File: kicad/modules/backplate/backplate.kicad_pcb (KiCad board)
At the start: 2 copper layers, 28 x 100 mm, 5 parts, among them J1 10018784-10210TLF

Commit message: update backplate libraries and schematic
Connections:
- J1 pad A10: unconnected-(J1-PadA10) -> +3.3V (x5)
- J1 pad A11: unconnected-(J1-PadA11) -> +3.3V (x5)
- J1 pad A12: unconnected-(J1-PadA12) -> +5V (x5)
- J1 pad A13: unconnected-(J1-PadA13) -> +5V (x5)
- J1 pad A14: unconnected-(J1-PadA14) -> +5V (x5)
- J1 pad A16: unconnected-(J1-PadA16) -> +7.4V (x5)
- J1 pad A17: unconnected-(J1-PadA17) -> +7.4V (x5)
- J1 pad A18: unconnected-(J1-PadA18) -> +7.4V (x5)
- J1 pad A2: unconnected-(J1-PadA2) -> CANP (x5)
- J1 pad A3: unconnected-(J1-PadA3) -> CANN (x5)
- J1 pad A4: unconnected-(J1-PadA4) -> GND (x5)
- J1 pad A5: unconnected-(J1-PadA5) -> GND (x5)
- J1 pad A6: unconnected-(J1-PadA6) -> GND (x5)
- J1 pad A7: unconnected-(J1-PadA7) -> GND (x5)
- J1 pad A9: unconnected-(J1-PadA9) -> +3.3V (x5)
- J1 pad B10: unconnected-(J1-PadB10) -> +3.3V (x5)
- J1 pad B11: unconnected-(J1-PadB11) -> +3.3V (x5)
- J1 pad B12: unconnected-(J1-PadB12) -> +5V (x5)
- J1 pad B13: unconnected-(J1-PadB13) -> +5V (x5)
- J1 pad B14: unconnected-(J1-PadB14) -> +5V (x5)
- J1 pad B16: unconnected-(J1-PadB16) -> +7.4V (x5)
- J1 pad B17: unconnected-(J1-PadB17) -> +7.4V (x5)
- J1 pad B18: unconnected-(J1-PadB18) -> +7.4V (x5)
- J1 pad B2: unconnected-(J1-PadB2) -> CANP (x5)
- J1 pad B3: unconnected-(J1-PadB3) -> CANN (x5)
- J1 pad B4: unconnected-(J1-PadB4) -> GND (x5)
- J1 pad B5: unconnected-(J1-PadB5) -> GND (x5)
- J1 pad B6: unconnected-(J1-PadB6) -> GND (x5)
- J1 pad B7: unconnected-(J1-PadB7) -> GND (x5)
- J1 pad B9: unconnected-(J1-PadB9) -> +3.3V (x5)

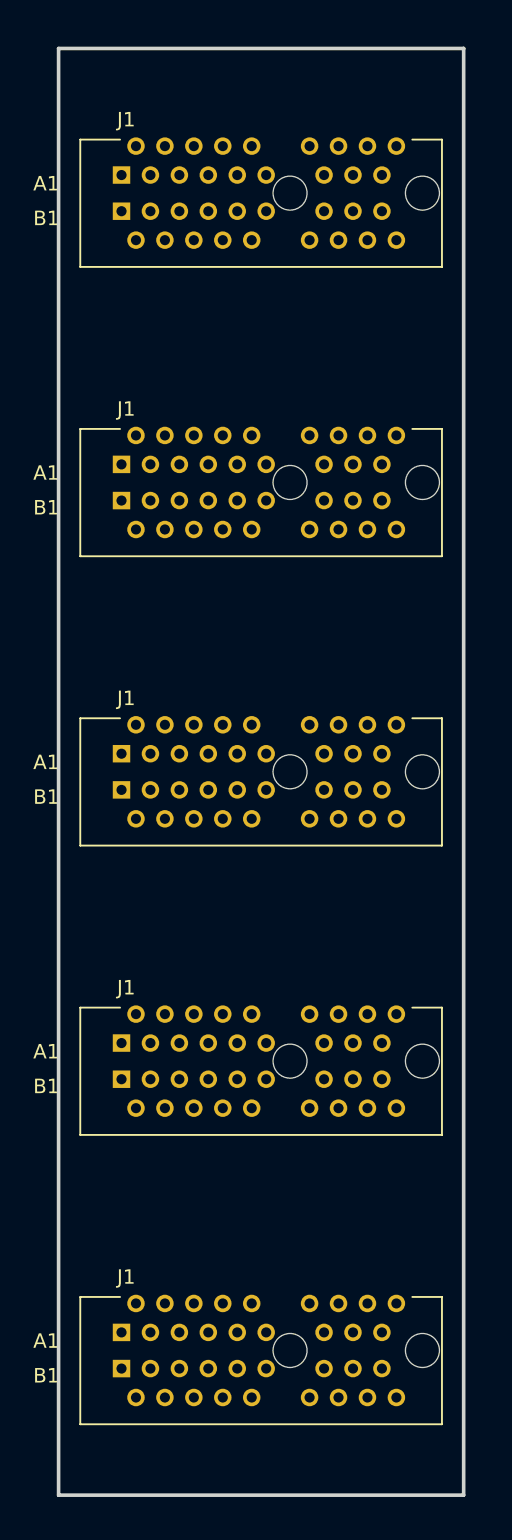
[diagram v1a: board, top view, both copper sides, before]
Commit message: update PCIe footprint; delete holes, and pads
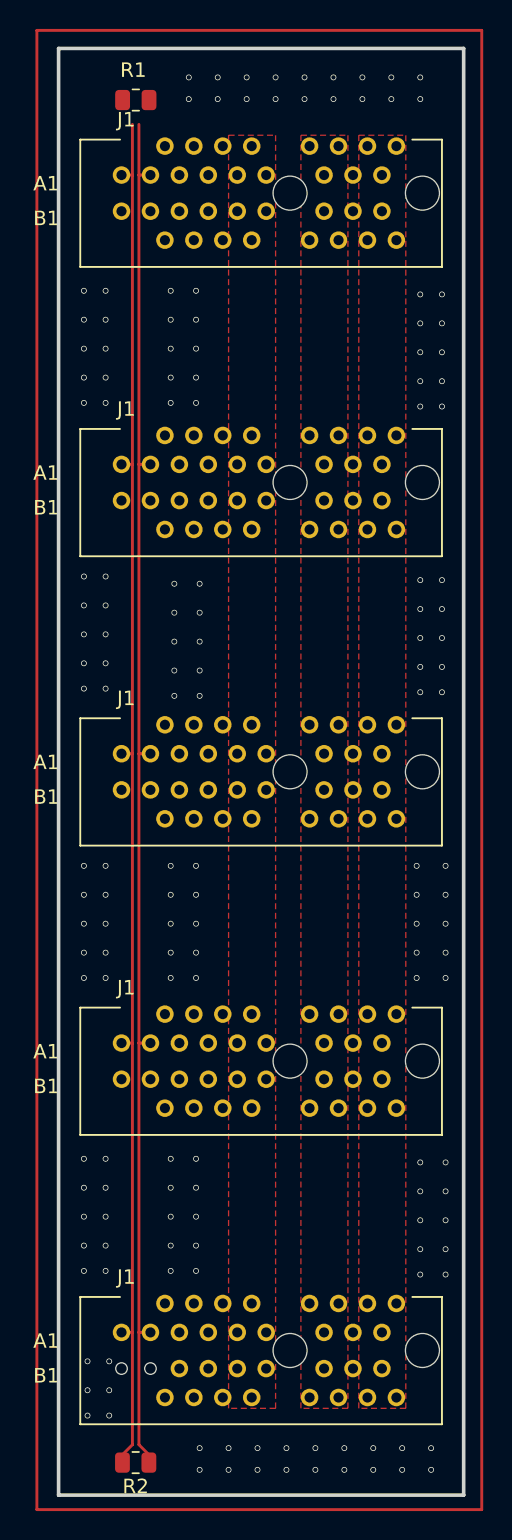
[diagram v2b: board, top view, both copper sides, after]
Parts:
- added R1: 120, Resistor_SMD:R_0805_2012Metric, F.Cu at (127.3, 53.6)
- added R2: 120, Resistor_SMD:R_0805_2012Metric, F.Cu at (127.3, 147.8)
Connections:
- J1 pad A1: unconnected-(J1-PadA1) -> CANN (x5)
- J1 pad A3: CANN -> CANP (x5)
- J1 pad B1: unconnected-(J1-PadB1) -> (no net) (x4)
- J1 pad B3: CANN -> (no net) (x4)
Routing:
- net CANP: track 0.00 -> 97.3 mm
- net CANN: track 0.00 -> 97.1 mm
- net GND: vias 0 -> 162
- added copper zone on F.Cu, net +3.3V
- added copper zone on F.Cu, net +5V
- added copper zone on F.Cu, net +7.4V
- added copper zone on B.Cu, net GND
- added copper zone on F.Cu, net GND

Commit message: test
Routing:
- net CANP: track 97.3 -> 1.05 mm
- net CANN: track 97.1 -> 1.05 mm
- net GND: vias 162 -> 160
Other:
- board text added: "backplate 0.1.0"
